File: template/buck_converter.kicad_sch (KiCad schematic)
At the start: 13 parts

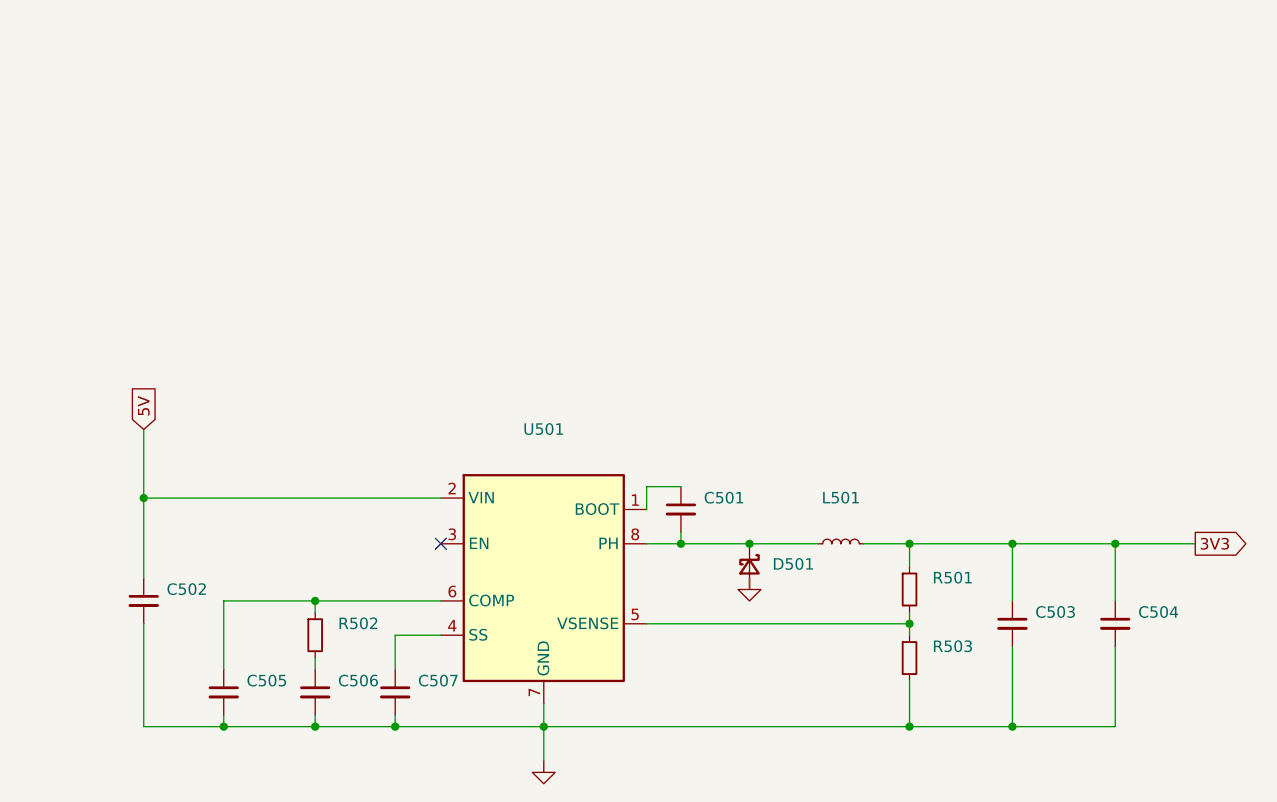
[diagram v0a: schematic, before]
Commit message: add template schematic (buck converter)
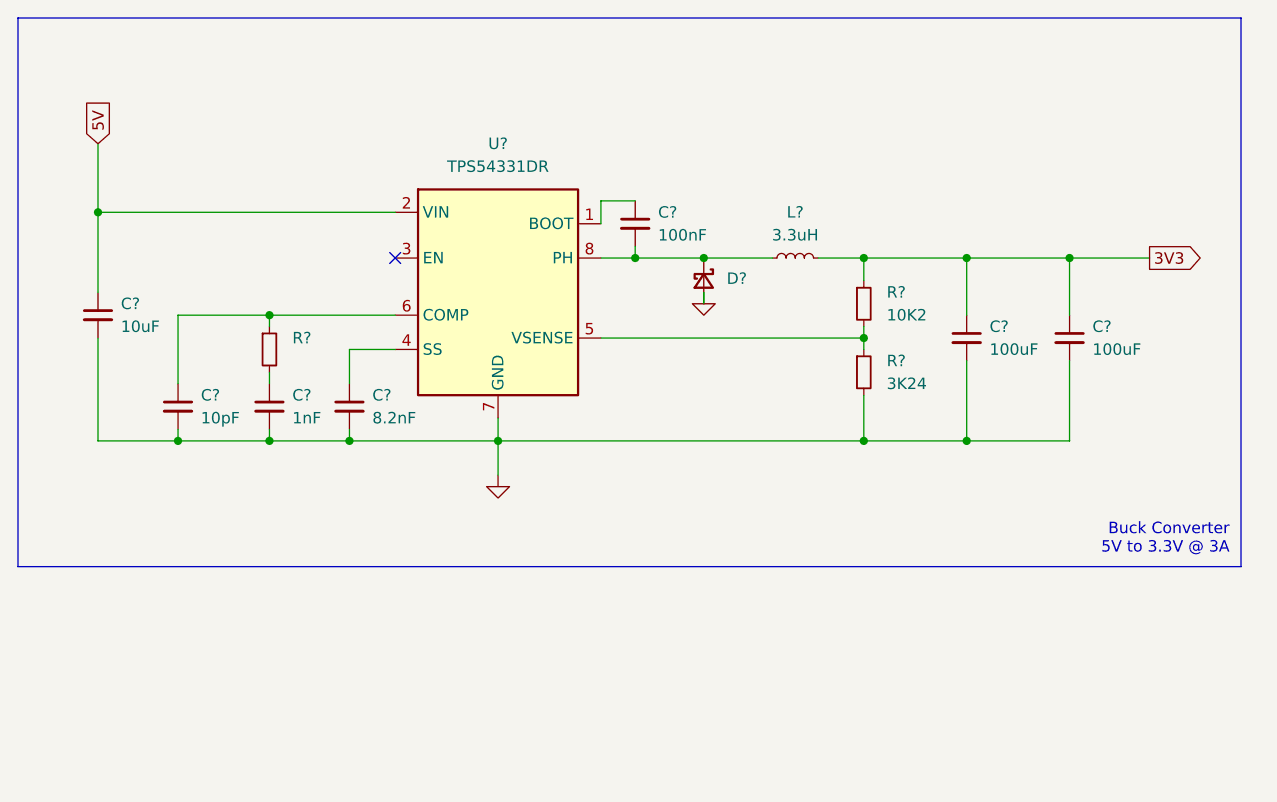
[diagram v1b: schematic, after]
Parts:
- C?: renamed from C503; value (none) -> 100uF
- C?: renamed from C506; value (none) -> 1nF
- C?: renamed from C507; value (none) -> 8.2nF
- C?: renamed from C502; value (none) -> 10uF
- C?: renamed from C504; value (none) -> 100uF
- C?: renamed from C501; value (none) -> 100nF
- C?: renamed from C505; value (none) -> 10pF
- D?: renamed from D501; value (none) -> 550mV/2A
- L?: renamed from L501; value (none) -> 3.3uH
- R?: renamed from R502; value (none) -> ~
- R?: renamed from R501; value (none) -> 10K2
- R?: renamed from R503; value (none) -> 3K24
- U?: renamed from U501; value (none) -> TPS54331DR
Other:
- note added: "Buck Converter 5V to 3.3V @ 3A"
- moved on the sheet: C?, D?, L?, R?, U?
